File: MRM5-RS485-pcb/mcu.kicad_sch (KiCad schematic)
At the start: 6 parts, among them U6 STM32L011F4Ux

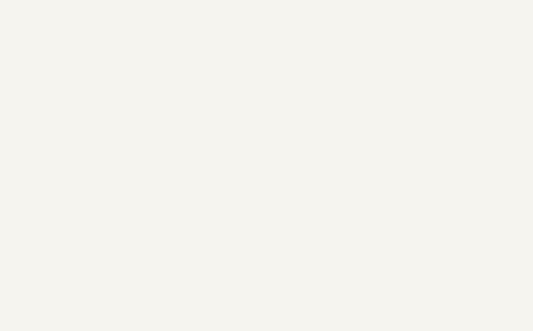
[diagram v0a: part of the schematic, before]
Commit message: logo added on pcb
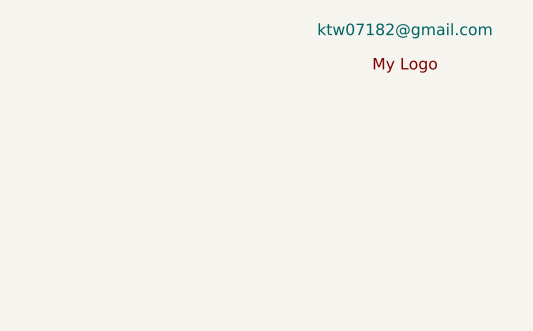
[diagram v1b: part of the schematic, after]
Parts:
- added Symbol1: ktw07182@gmail.com, Mouser:ktw07182_logo, symbol Mouser:MyLogo
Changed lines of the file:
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@@
+	)
+	(symbol
+		(lib_id "Mouser:MyLogo")
+		(at 267.97 26.67 0)
+		(unit 1)
+		(exclude_from_sim no)
+		(in_bom no)
+		(on_board yes)
+		(dnp no)
+		(fields_autoplaced yes)
+		(property "Reference" "Symbol1"
+			(at 267.97 26.67 0)
+			(effects
+				(font
+					(size 1.27 1.27)
+				)
+				(hide yes)
+			)
+		)
+		(property "Value" "ktw07182@gmail.com"
+			(at 267.208 20.32 0)
+			(effects
+				(font
+					(size 1.27 1.27)
+				)
+			)
+		)
+		(property "Footprint" "Mouser:ktw07182_logo"
+			(at 267.97 26.67 0)
+			(effects
+				(font
+					(size 1.27 1.27)
+				)
+				(hide yes)
+			)
+		)
+		(property "Datasheet" ""
+			(at 267.97 26.67 0)
+			(effects
+				(font
+					(size 1.27 1.27)
+				)
+				(hide yes)
+			)
+		)
+		(property "Description" ""
+			(at 267.97 26.67 0)
+			(effects
+				(font
+					(size 1.27 1.27)
+				)
+				(hide yes)
+			)
+		)
+		(instances
+			(project "MRM5-RS485-pcb"
+				(path "/26277d8d-227e-42ba-8f6b-65f74e4d2de8/ee386eb0-6141-4f55-88e0-a1798f176fab"
+					(reference "Symbol1")
+					(unit 1)
+				)
+			)
+		)
 	)
 	(symbol
